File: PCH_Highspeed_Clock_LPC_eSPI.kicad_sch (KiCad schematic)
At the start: 1 part

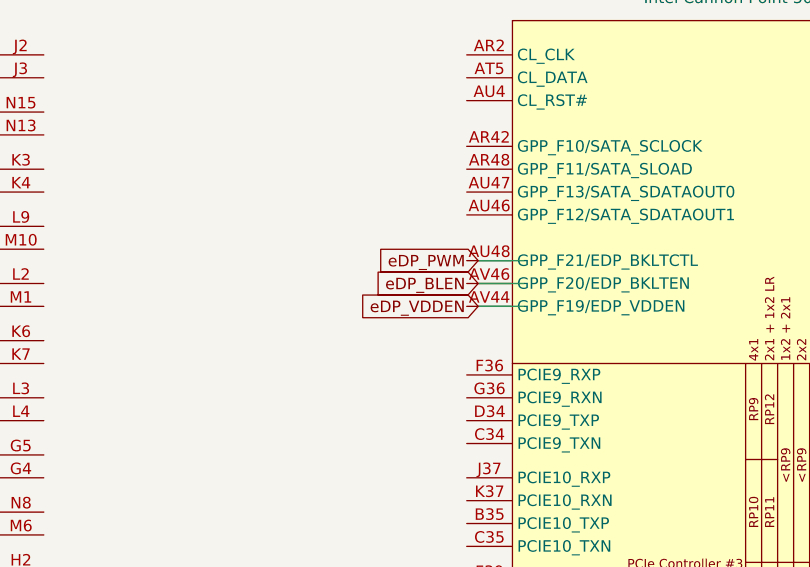
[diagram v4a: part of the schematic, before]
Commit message: Fixed 2 pins that somehow disappeared from schematic
i blame my kicad libraries being weird lol
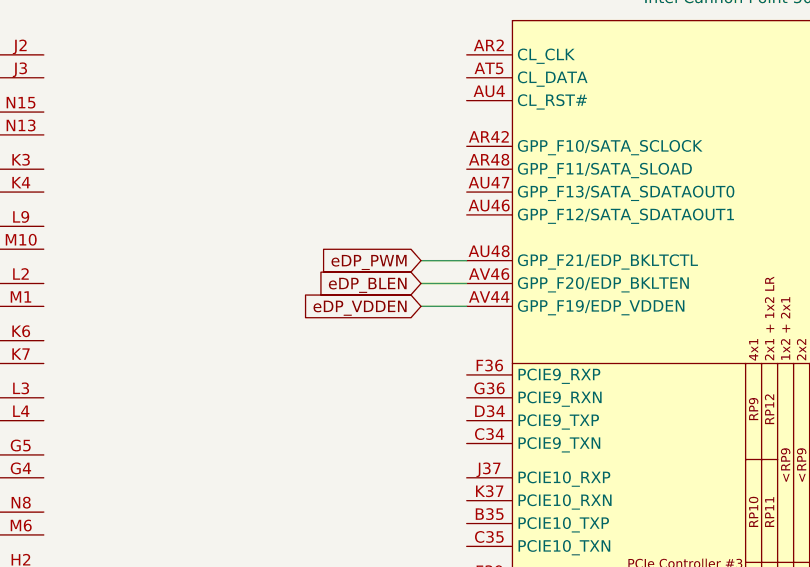
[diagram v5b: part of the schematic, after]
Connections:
- net eDP_BLEN: now also UPCH1.AV46 (GPP_F20/EDP_BKLTEN)
- net eDP_PWM: now also UPCH1.AU48 (GPP_F21/EDP_BKLTCTL)
- net eDP_VDDEN: now also UPCH1.AV44 (GPP_F19/EDP_VDDEN)
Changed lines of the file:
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@@
 	(wire
 		(pts
-			(xy 180.34 57.15) (xy 185.42 57.15)
+			(xy 173.99 57.15) (xy 179.07 57.15)
 		)
 		(stroke
@@
 	(wire
 		(pts
-			(xy 180.34 52.07) (xy 185.42 52.07)
+			(xy 173.99 52.07) (xy 179.07 52.07)
 		)
 		(stroke
@@
 	(wire
 		(pts
-			(xy 180.34 54.61) (xy 185.42 54.61)
+			(xy 173.99 54.61) (xy 179.07 54.61)
 		)
 		(stroke
@@
 	(global_label "eDP_VDDEN"
 		(shape input)
-		(at 180.34 57.15 180)
+		(at 173.99 57.15 180)
 		(fields_autoplaced yes)
 		(effects
@@
 		)
 		(property "Intersheetrefs" "${INTERSHEET_REFS}"
-			(at 159.8771 57.15 0)
+			(at 153.5271 57.15 0)
 			(effects
 				(font
@@
 	(global_label "eDP_PWM"
 		(shape input)
-		(at 180.34 52.07 180)
+		(at 173.99 52.07 180)
 		(fields_autoplaced yes)
 		(effects
@@
 		)
 		(property "Intersheetrefs" "${INTERSHEET_REFS}"
-			(at 159.8771 52.07 0)
+			(at 153.5271 52.07 0)
 			(effects
 				(font
@@
 	(global_label "eDP_BLEN"
 		(shape input)
-		(at 180.34 54.61 180)
+		(at 173.99 54.61 180)
 		(fields_autoplaced yes)
 		(effects
@@
 		)
 		(property "Intersheetrefs" "${INTERSHEET_REFS}"
-			(at 159.8771 54.61 0)
+			(at 153.5271 54.61 0)
 			(effects
 				(font
@@
 		(pin "G2"
 		)
+		(pin "AN35"
+		)
+		(pin "AL37"
+		)
 		(instances
 			(project "Stroopwafel-LGA1151-CFL"
@@
 					(unit 7)
 				)
+				(path "/4bc771b8-eb19-46d0-8798-27231a7c6e83/cd978078-9495-426d-921d-88f146c11707"
+					(reference "UPCH1")
+					(unit 7)
+				)
 			)
 		)
@@
 		(pin "G2"
 		)
+		(pin "AN35"
+		)
+		(pin "AL37"
+		)
 		(instances
 			(project "Stroopwafel-LGA1151-CFL"
@@
 					(unit 13)
 				)
+				(path "/4bc771b8-eb19-46d0-8798-27231a7c6e83/cd978078-9495-426d-921d-88f146c11707"
+					(reference "UPCH1")
+					(unit 13)
+				)
 			)
 		)
@@
 		(pin "G2"
 		)
+		(pin "AN35"
+		)
+		(pin "AL37"
+		)
 		(instances
 			(project "Stroopwafel-LGA1151-CFL"
@@
 					(unit 3)
 				)
+				(path "/4bc771b8-eb19-46d0-8798-27231a7c6e83/cd978078-9495-426d-921d-88f146c11707"
+					(reference "UPCH1")
+					(unit 3)
+				)
 			)
 		)
@@
 		(pin "G2"
 		)
+		(pin "AN35"
+		)
+		(pin "AL37"
+		)
 		(instances
 			(project "Stroopwafel-LGA1151-CFL"
@@
 					(unit 6)
 				)
+				(path "/4bc771b8-eb19-46d0-8798-27231a7c6e83/cd978078-9495-426d-921d-88f146c11707"
+					(reference "UPCH1")
+					(unit 6)
+				)
 			)
 		)
@@
 		(pin "G2"
 		)
+		(pin "AL37"
+		)
+		(pin "AN35"
+		)
 		(instances
 			(project "Stroopwafel-LGA1151-CFL"
@@
 					(reference "UPCH1")
 					(unit 2)
+				)
+				(path "/4bc771b8-eb19-46d0-8798-27231a7c6e83/cd978078-9495-426d-921d-88f146c11707"
+					(reference "UPCH1")
+					(unit 2)

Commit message: implemented some misc cpu signals
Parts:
- added R38: 619Ω, Resistor_SMD:R_0402_1005Metric, symbol Device:R_Small
- added R41: 1kΩ, Resistor_SMD:R_0402_1005Metric, symbol Device:R_Small
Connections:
- net at UPCH1.AD3 (THRMTRIP#): now also R38.1
- net PM_DOWN_PCH: now reaches UPCH1.AE2 (PM_DOWN)
- net PECI_PCH: now reaches UPCH1.AF2 (PECI)
- net PECI_PCH: now also R41.2
- net PM_SYNC_PCH: now reaches UPCH1.AF3 (PM_SYNC)
- net PLTRST_CPU#: now reaches UPCH1.AG5 (PLTRST_CPU#)
- new net GND: R41.1
- new net THERMTRIP#: R38.2

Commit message: idek what i changed anymore but there's a bunch of new stuff lol
iirc i did some more misc cpu pins and a bunch of pch pcie stuff
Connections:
- net SSD0_Refclk+: now reaches UPCH1.AH10 (CLKOUT_PCIE_P1)
- net SSD0_Refclk-: now reaches UPCH1.AH9 (CLKOUT_PCIE_N1)
- net SSD0_CLKREQ#: now reaches UPCH1.BE31 (GPP_B6/SRCCLKREQ1#)
- net SSD0_PCIe_Tx2+: now reaches UPCH1.B35 (PCIE10_TXP)
- net SSD0_PCIe_Tx1-: now reaches UPCH1.B36 (PCIE11_TXN/SATA0A_TXN)
- net SSD0_PCIe_Tx3-: now reaches UPCH1.C34 (PCIE9_TXN)
- net SSD0_PCIe_Tx2-: now reaches UPCH1.C35 (PCIE10_TXN)
- net SSD0_PCIe_Tx1+: now reaches UPCH1.C36 (PCIE11_TXP/SATA0A_TXP)
- net SSD0_PCIe_Tx3+: now reaches UPCH1.D34 (PCIE9_TXP)
- net SSD0_PCIe/SATA_Tx0-: now reaches UPCH1.D38 (PCIE12_TXN/SATA1A_TXN)
- net SSD0_PCIe/SATA_Tx0+: now reaches UPCH1.E37 (PCIE12_TXP/SATA1A_TXP)
- net SSD0_PCIe_Rx3+: now reaches UPCH1.F36 (PCIE9_RXP)
- net SSD0_PCIe_Rx1+: now reaches UPCH1.F39 (PCIE11_RXP/SATA0A_RXP)
- net SSD0_PCIe_Rx3-: now reaches UPCH1.G36 (PCIE9_RXN)
- net SSD0_PCIe_Rx1-: now reaches UPCH1.G38 (PCIE11_RXN/SATA0A_RXN)
- net SSD0_PCIe/SATA_Rx0-: now reaches UPCH1.H42 (PCIE12_RXN/SATA1A_RXN)
- net SSD0_PCIe_Rx2+: now reaches UPCH1.J37 (PCIE10_RXP)
- net SSD0_PCIe/SATA_Rx0+: now reaches UPCH1.J41 (PCIE12_RXP/SATA1A_RXP)
- net SSD0_PCIe_Rx2-: now reaches UPCH1.K37 (PCIE10_RXN)
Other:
- note added: "PCIe controller 1 (L1-4): ? PCIe controller 2 (L5-8): ? PCIe controller 3 (L9-12): NVMe 0 with lane reversal for SATA on first lane x2 no SATA on H310, x4 with SATA on all other chipsets PCIe controller 4 (L13-16): ? PCIe controller 5 (L17-20): ? PCIe controller 6 (L21-24): ?"
- note added: "subtract 5 for PCIe lane number (first 6 lanes are the USB3.2G2 ports + index starts at 0 vs 1)"
- moved on the sheet: R38, R41, UPCH1G
